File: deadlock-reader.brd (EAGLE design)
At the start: 49.2 x 49.5 mm, 49 parts, among them IC1 LM386M-1, IC2 STM32F072XX, IC3 MCP16301/H, IC4 MAX3232CSE, J1 RJ12 6p6c, X1 MINI-USB-SCHIELD-32005-301

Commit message: Optimize component placements
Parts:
- moved JP3 41.4 mm to (47.0, 26.7), flipped to the bottom, turned to 270 degrees
- moved R6 27.7 mm to (35.6, 24.1), turned to 90 degrees
- moved C10 23.4 mm to (22.9, 15.2), turned to 0 degrees
- moved C11 21.7 mm to (27.3, 15.2), turned to 0 degrees
- moved C14 21.0 mm to (31.8, 15.2)
- moved C12 19.8 mm to (43.2, 29.2), turned to 180 degrees
- moved R7 19.1 mm to (21.6, 45.7), turned to 180 degrees
- moved R8 18.2 mm to (21.6, 38.1), turned to 180 degrees
- moved R9 13.7 mm to (21.6, 40.6), turned to 180 degrees
- moved IC4 12.0 mm to (26.7, 21.6), turned to 0 degrees
- moved R10 10.5 mm to (21.6, 43.2), turned to 180 degrees
- moved C8 9.92 mm to (20.3, 7.62), flipped to the top, turned to 90 degrees
- moved C9 9.67 mm to (24.1, 7.62), flipped to the top, turned to 90 degrees
- moved IC1 8.89 mm to (35.6, 8.89), turned to 270 degrees
- moved IC2 8.89 mm to (35.6, 31.8), turned to 90 degrees
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
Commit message: Final component placement
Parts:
- C5: value 220uF -> 100uF; device rcl:PANASONIC_D -> rcl:C1206
- moved SP1 40.2 mm to (43.2, 42.5)
- moved IC1 31.9 mm to (32.4, 40.6), turned to 90 degrees
- moved C5 30.5 mm to (45.1, 39.4), turned to 0 degrees
- moved R11 28.6 mm to (43.2, 3.17), flipped to the bottom
- moved C12 27.5 mm to (22.2, 47.0), turned to 0 degrees
- moved L1 24.4 mm to (43.2, 10.2), turned to 180 degrees
- moved C4 24.3 mm to (40.0, 39.4), turned to 0 degrees
- moved D5 24.3 mm to (29.8, 6.99), turned to 0 degrees
- moved R12 22.9 mm to (40.6, 3.17), flipped to the bottom
- moved C8 21.7 mm to (40.6, 15.2), flipped to the bottom, turned to 180 degrees
- moved R5 20.8 mm to (34.9, 36.2)
- moved C9 19.1 mm to (40.6, 17.1), flipped to the bottom, turned to 180 degrees
- moved IC3 17.7 mm to (37.5, 3.17)
- moved D2 16.8 mm to (22.2, 22.9), turned to 270 degrees
- moved C13 16.3 mm to (22.9, 8.89), flipped to the bottom, turned to 270 degrees
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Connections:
- net N$16: now also C5.1; no longer C5.+
- net N$18: now also C5.2; no longer C5.-

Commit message: [WIP] Route the power converter
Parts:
- moved IC2 2.77 mm to (33.0, 29.1)
- moved D3 2.62 mm to (38.1, 10.2)
- moved C2 2.62 mm to (33.0, 31.1)
- moved C3 2.50 mm to (33.0, 29.1)
- moved C1 2.38 mm to (33.0, 27.1)
- moved IC3 2.01 mm to (36.8, 5.08)
- moved C6 2.01 mm to (34.9, 12.1)
- moved C9 2.01 mm to (40.0, 19.1)
- moved D5 2.01 mm to (29.2, 8.89)
- moved R11 2.01 mm to (42.5, 5.08), turned to 270 degrees
- moved R12 2.01 mm to (40.0, 5.08)
- moved C8 2.01 mm to (40.0, 17.1)
- moved L1 2.01 mm to (42.5, 12.1)
- moved C7 1.42 mm to (33.7, 4.45)
- moved D4 1.27 mm to (31.8, 4.45)
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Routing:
- net +3V3: track 0.00 -> 74.3 mm, vias 0 -> 3
- net RDR_TXD/SWDIO: track 0.00 -> 37.8 mm, vias 0 -> 1
- net N$9: track 0.00 -> 36.3 mm
- net RDR_RXD: track 0.00 -> 26.2 mm, vias 0 -> 1
- net GND: track 0.00 -> 20.6 mm, vias 0 -> 3
- net T_SWO: track 0.00 -> 15.5 mm
- net N$25: track 0.00 -> 12.3 mm
- net SWCLK: track 0.00 -> 10.8 mm
- net V+: track 0.00 -> 8.51 mm
- net N$23: track 0.00 -> 7.41 mm
- net N$22: track 0.00 -> 4.78 mm
- added copper zone on layer 16, net +3V3
- added copper zone on layer 1, net GND
- added copper zone on layer 16, net GND
- added copper zone on layer 16, net N$22

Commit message: [WIP] Fix DRC errors on power converter layout
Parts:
- moved JP3 2.25 mm to (45.7, 28.5)
- moved C4 0.52 mm to (40.5, 39.4), turned to 180 degrees
- moved IC1 0.35 mm to (32.1, 40.9), turned to 270 degrees
- moved C10 0.25 mm to (25.0, 8.89)
- moved C11 0.25 mm to (25.0, 13.3)
- moved R15 0.25 mm to (14.0, 23.1)
- moved R13 0.12 mm to (14.0, 27.4)
- moved R14 0.12 mm to (14.0, 25.3)
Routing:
- net RDR_TXD/SWDIO: track 37.8 -> 0.00 mm, vias 1 -> 0
- net RDR_RXD: track 26.2 -> 0.00 mm, vias 1 -> 0
- net +3V3: track 74.3 -> 57.6 mm
- net T_SWO: track 15.5 -> 0.00 mm
- net N$16: track 0.00 -> 10.9 mm
- net SWCLK: track 10.8 -> 0.00 mm
- net GND: track 20.6 -> 10.7 mm
- net N$17: track 0.00 -> 5.01 mm
- net N$18: track 0.00 -> 3.23 mm
- net N$9: track 36.3 -> 34.2 mm

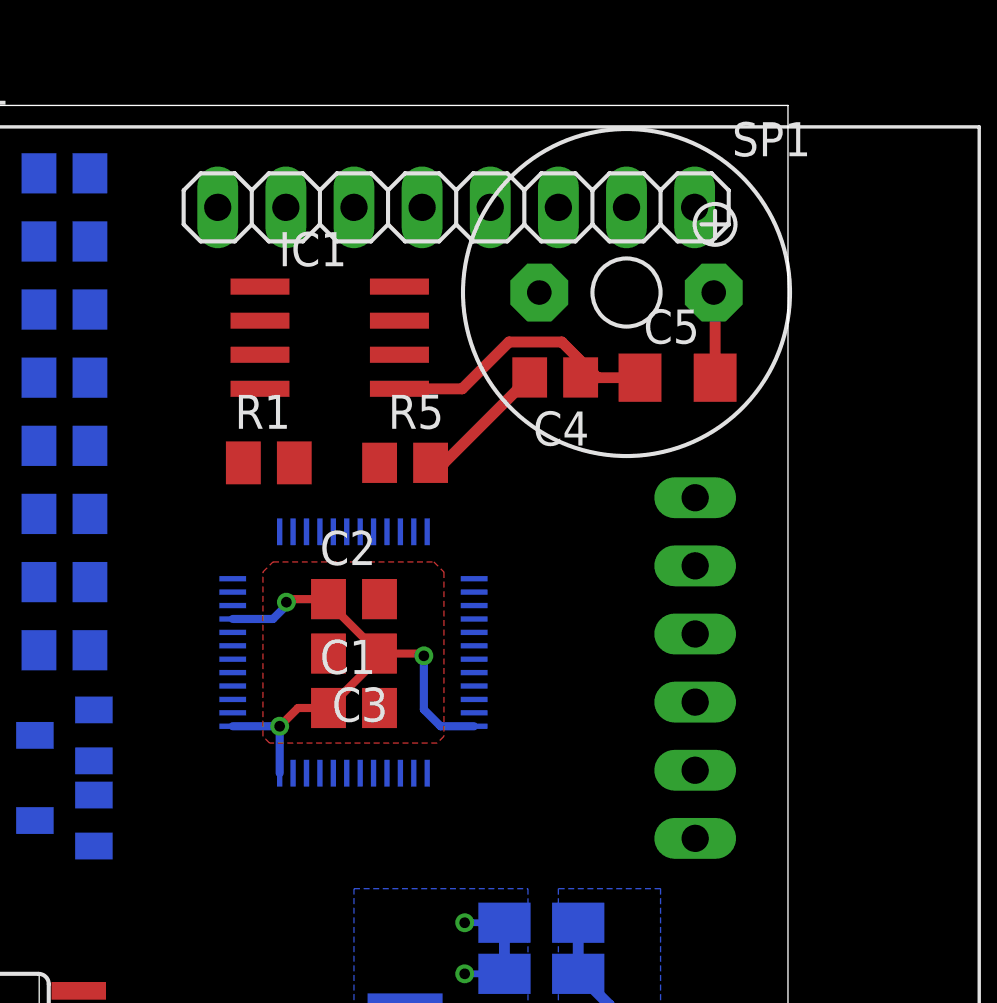
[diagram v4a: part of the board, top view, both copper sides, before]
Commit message: [WIP] Route debug and RFID connectors to the MCU
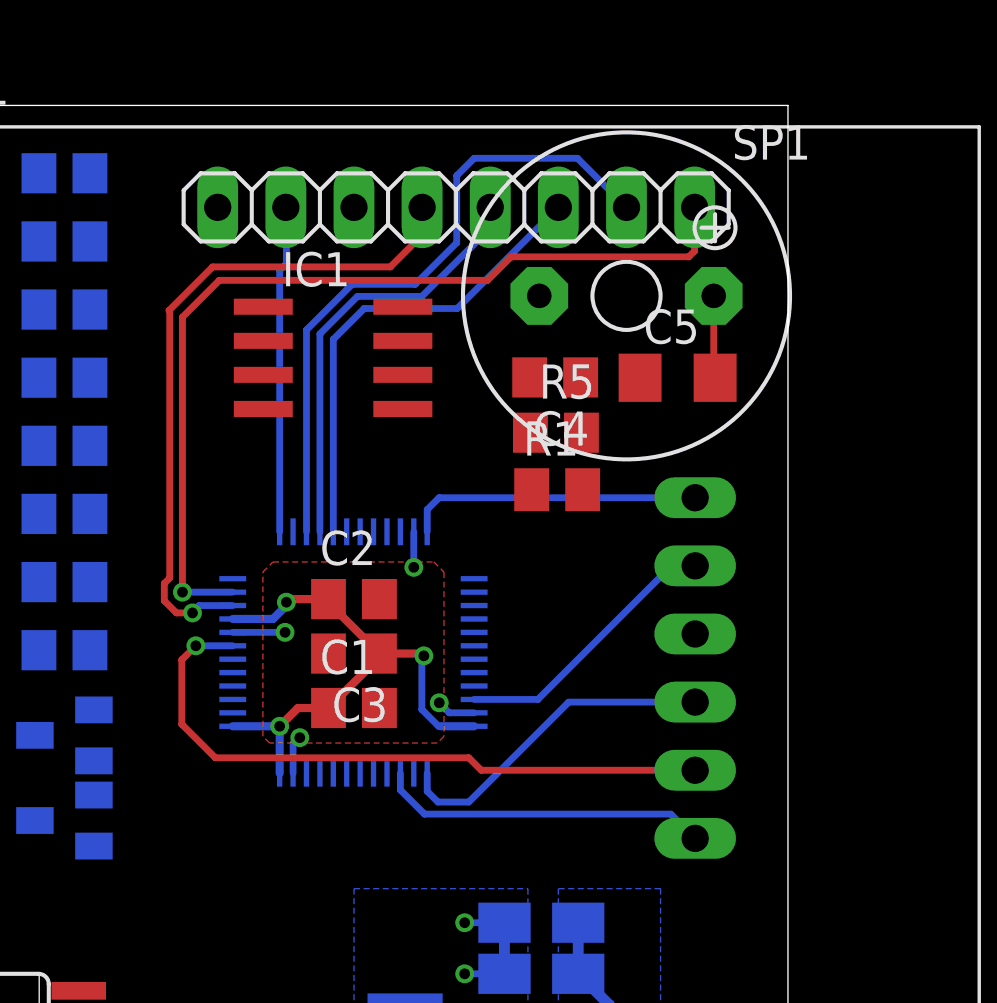
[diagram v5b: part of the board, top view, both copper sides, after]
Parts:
- moved R1 10.8 mm to (40.6, 35.2)
- moved R5 5.74 mm to (40.5, 37.3)
- moved IC1 0.76 mm to (32.2, 40.1)
- moved SP1 0.12 mm to (43.2, 42.4)
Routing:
- net RFID_SS: track 0.00 -> 33.9 mm, vias 0 -> 1
- net RFID_IRQ: track 0.00 -> 25.4 mm, vias 0 -> 1
- net RST: track 0.00 -> 24.4 mm, vias 0 -> 1
- net RFID_SCK: track 0.00 -> 24.3 mm
- net RFID_MOSI: track 0.00 -> 17.6 mm
- net RFID_MISO: track 0.00 -> 16.1 mm
- net RDR_TXD/SWDIO: track 0.00 -> 12.4 mm
- net T_SWO: track 0.00 -> 12.4 mm
- net RFID_RST: track 0.00 -> 12.2 mm
- net +3V3: track 57.6 -> 68.7 mm
- net N$16: track 10.9 -> 0.00 mm
- net SWCLK: track 0.00 -> 10.3 mm
- net GND: track 10.7 -> 16.9 mm, vias 3 -> 7
- net N$17: track 5.01 -> 0.00 mm

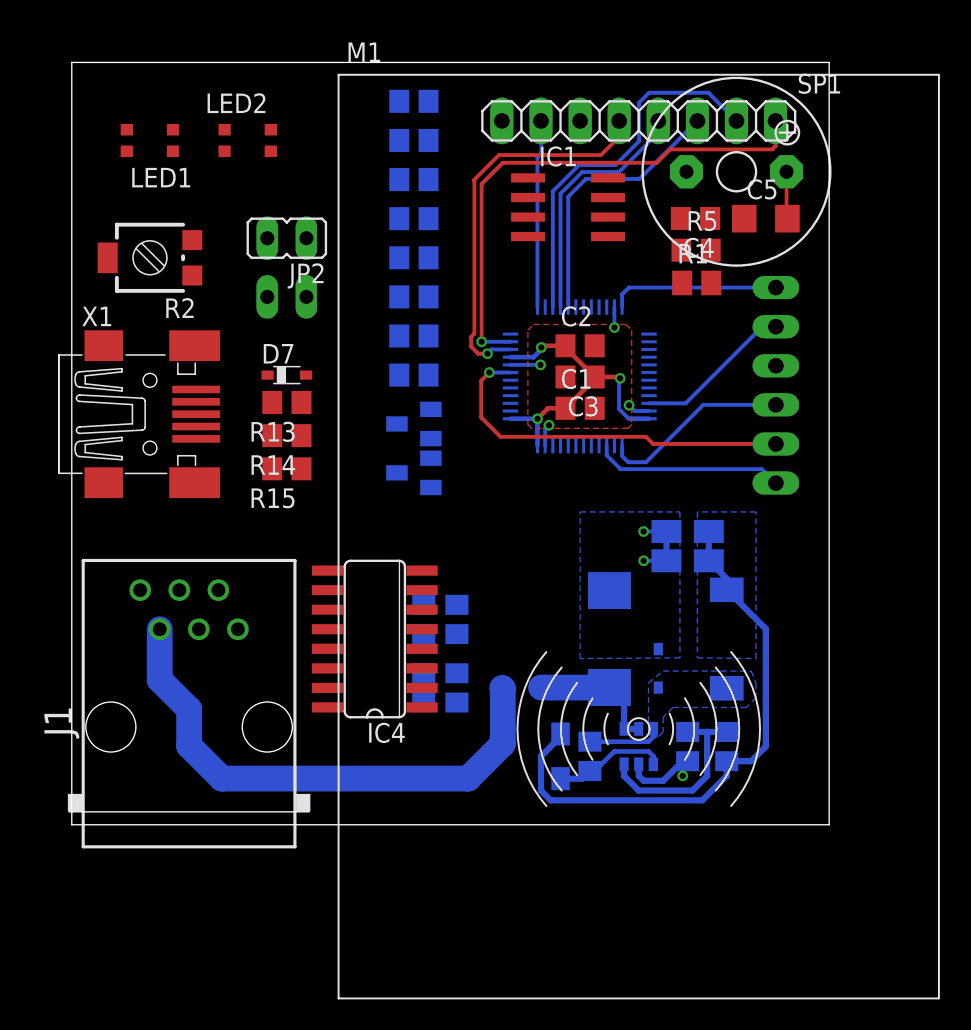
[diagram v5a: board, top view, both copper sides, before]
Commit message: [WIP] Route leds and audio interface
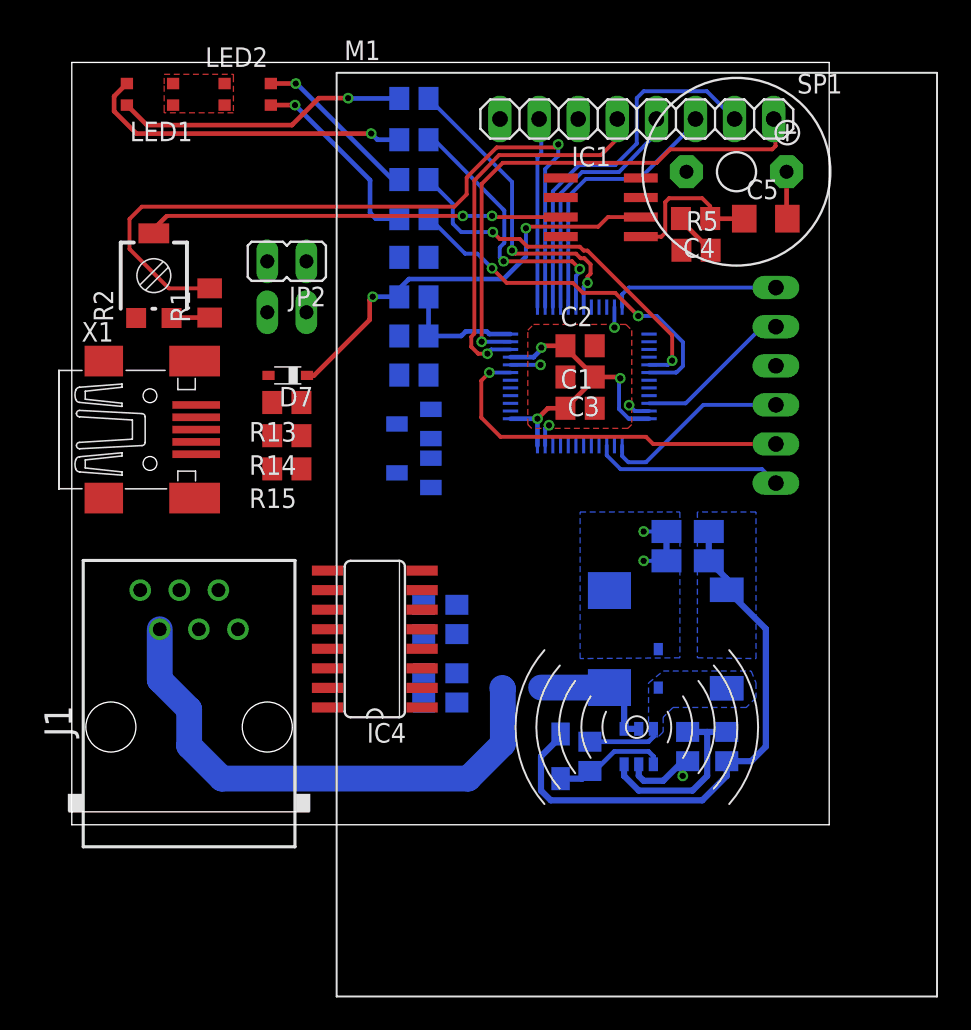
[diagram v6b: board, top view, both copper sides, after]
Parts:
- moved R1 31.7 mm to (8.96, 33.9), turned to 90 degrees
- moved R8 10.4 mm to (22.2, 47.2)
- moved C12 10.1 mm to (22.2, 36.9), turned to 180 degrees
- moved LED1 3.00 mm to (5.08, 47.5)
- moved LED2 3.00 mm to (11.4, 47.5)
- moved IC1 2.12 mm to (34.4, 40.1)
- moved JP2 1.50 mm to (14.0, 36.6)
- moved R2 1.19 mm to (5.33, 35.7), turned to 0 degrees
- moved JP1 1.00 mm to (14.0, 33.3)
- moved X1 1.00 mm to (5.08, 25.7)
- moved M1 0.18 mm to (36.7, 45.8)
- moved D7 0.06 mm to (14.0, 29.2), turned to 180 degrees
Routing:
- net AUDIO_OUT: track 0.00 -> 49.6 mm, vias 0 -> 1
- net V+: track 8.51 -> 36.6 mm, vias 0 -> 2
- net N$15: track 0.00 -> 27.1 mm, vias 0 -> 2
- net LED_G2: track 0.00 -> 24.0 mm, vias 0 -> 2
- net LED_R2: track 0.00 -> 23.8 mm, vias 0 -> 2
- net N$19: track 0.00 -> 21.4 mm, vias 0 -> 1
- net LED_G1: track 0.00 -> 20.6 mm, vias 0 -> 2
- net N$20: track 0.00 -> 19.0 mm, vias 0 -> 1
- net LED_R1: track 0.00 -> 18.4 mm, vias 0 -> 2
- net N$10: track 0.00 -> 12.6 mm, vias 0 -> 1
- net N$21: track 0.00 -> 10.9 mm, vias 0 -> 1
- net N$16: track 0.00 -> 9.95 mm
- net V_SENSE: track 0.00 -> 8.06 mm
- net N$17: track 0.00 -> 2.86 mm
- net N$14: track 0.00 -> 2.49 mm

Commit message: [WIP] Route RS-232 and USB interfaces
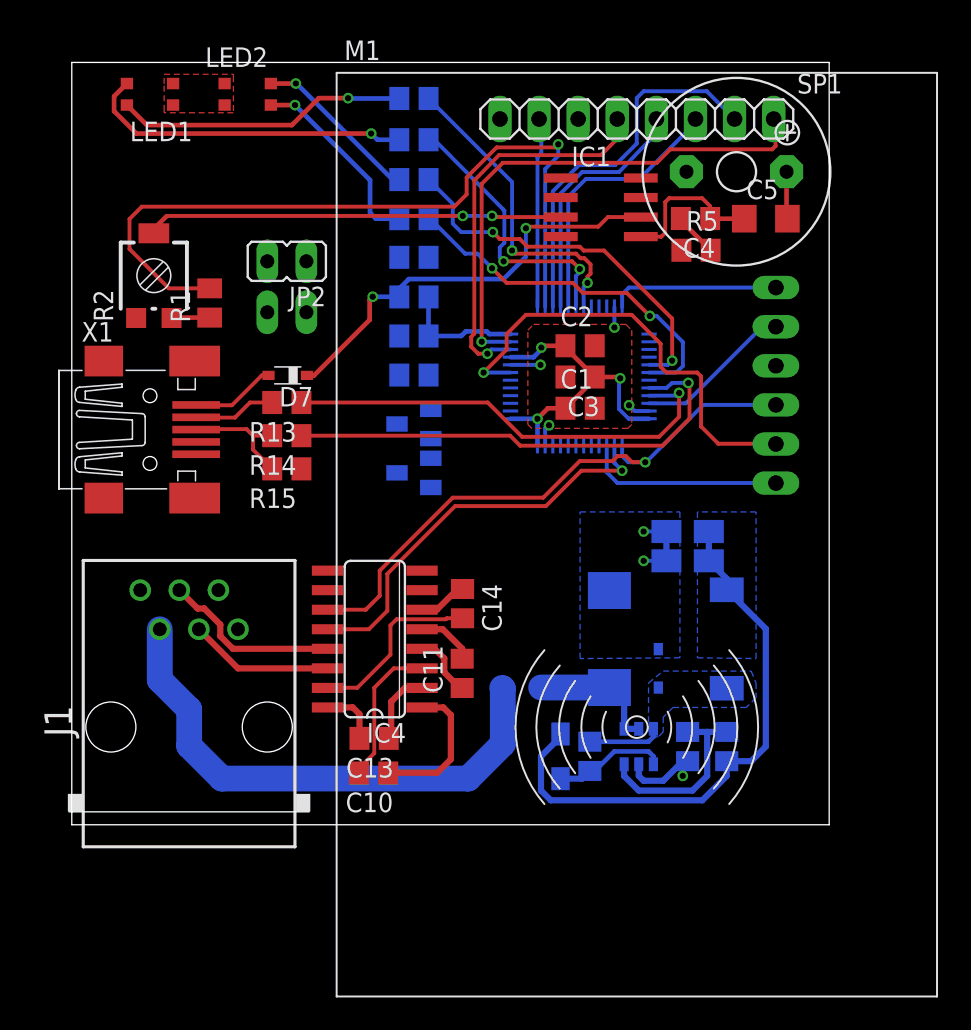
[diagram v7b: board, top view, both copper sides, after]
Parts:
- moved C10 7.73 mm to (19.6, 3.36), flipped to the top, turned to 180 degrees
- moved C13 4.60 mm to (19.6, 5.61), flipped to the top, turned to 180 degrees
- moved C11 3.52 mm to (25.4, 9.84), flipped to the top
- moved C14 2.73 mm to (25.4, 14.4), flipped to the top, turned to 270 degrees
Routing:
- net USB_D+: track 0.00 -> 31.2 mm, vias 0 -> 1
- net USB_D-: track 0.00 -> 29.8 mm, vias 0 -> 1
- net RDR_RXD: track 0.00 -> 26.6 mm, vias 0 -> 1
- net RDR_TXD/SWDIO: track 12.4 -> 38.3 mm, vias 0 -> 1
- net GND: track 16.9 -> 28.6 mm
- net N$1: track 0.00 -> 11.6 mm
- net N$4: track 0.00 -> 9.59 mm
- net N$2: track 0.00 -> 9.41 mm
- net N$3: track 0.00 -> 9.38 mm
- net N$13: track 0.00 -> 7.80 mm
- net N$11: track 0.00 -> 5.51 mm
- net N$12: track 0.00 -> 5.35 mm
- net N$7: track 0.00 -> 4.83 mm
- net RST: track 24.4 -> 29.1 mm
- net N$5: track 0.00 -> 4.18 mm
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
